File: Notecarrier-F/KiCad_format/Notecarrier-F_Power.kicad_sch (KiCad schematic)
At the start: 48 parts, among them J1 S2BPHSM4TBLFSN, J2 S2BPHSM4TBLFSN, J3 S2BPHSM4TBLFSN, J4 10118193-0001LF, U1 TPS62748YFPT, U2 BQ24210DQCT, U3 TPS63020DSJR, U5 MAX17225ELT+

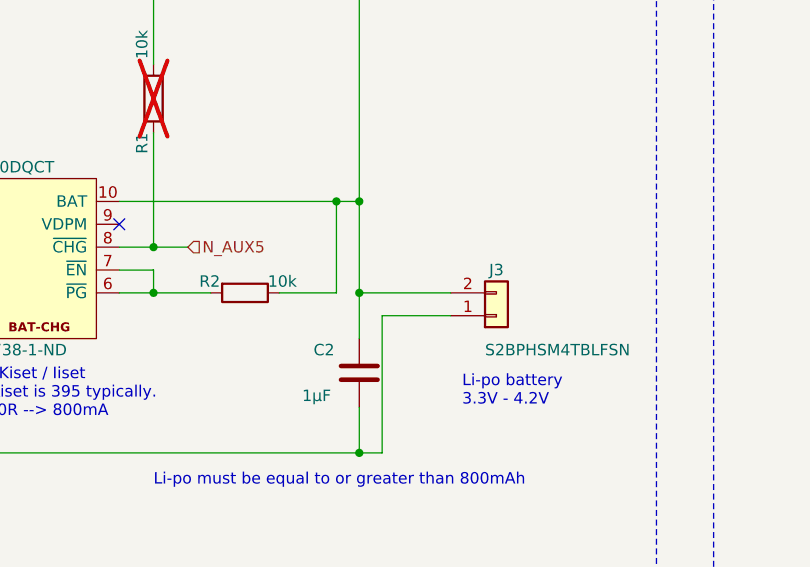
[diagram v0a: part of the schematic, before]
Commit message: Correct BQ24210DQCT BAT pin to Power Input.
Realised it was incorrectly specified as a Power Output while porting Notecarrier-A. It’s the battery itself which is the source of power, so even though this pin provides charging current, it must be a Power Input since it is connected to the Power Output of the battery. The symbol has been fixed, so I updated it and put the PWR_FLAG where it should be - at the battery.
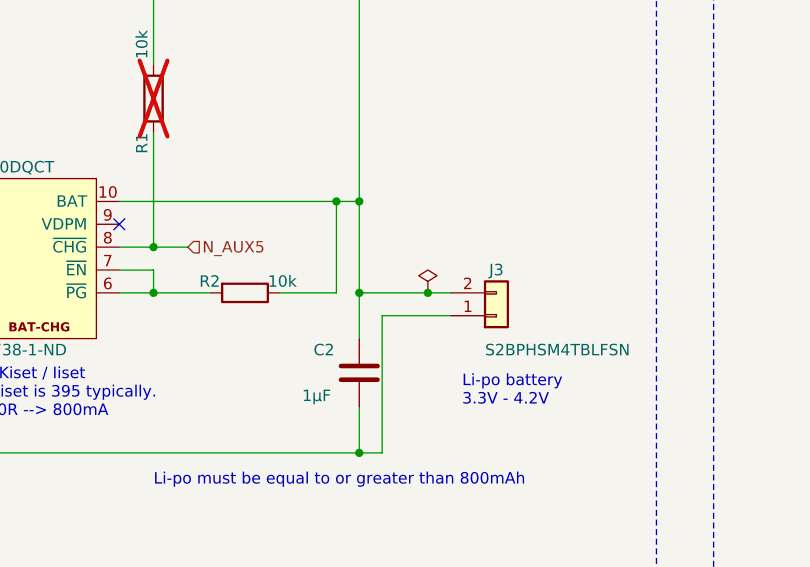
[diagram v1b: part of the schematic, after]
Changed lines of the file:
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@@
   (junction (at 257.81 71.12) (diameter 0) (color 0 0 0 0)
+  )
+  (junction (at 153.67 135.89) (diameter 0) (color 0 0 0 0)
   )
   (junction (at 309.88 170.18) (diameter 0) (color 0 0 0 0)
@@
     (stroke (width 0) (type default))
   )
-  (wire (pts (xy 146.05 135.89) (xy 156.21 135.89))
+  (wire (pts (xy 146.05 135.89) (xy 153.67 135.89))
     (stroke (width 0) (type default))
   )
@@
   )
   (wire (pts (xy 322.58 160.02) (xy 313.69 160.02))
+    (stroke (width 0) (type default))
+  )
+  (wire (pts (xy 153.67 135.89) (xy 156.21 135.89))
     (stroke (width 0) (type default))
   )
@@
         )
       )
+    )
+  )
+  (symbol (lib_id "power:PWR_FLAG") (at 153.67 135.89 0) (unit 1)
+    (in_bom yes) (on_board yes) (dnp no) (fields_autoplaced)
+    (property "Reference" "#FLG012" (at 153.67 133.985 0)
+      (effects (font (size 1.27 1.27)) hide)
+    )
+    (property "Value" "PWR_FLAG" (at 153.67 132.08 0)
+      (effects (font (size 1.27 1.27)) hide)
+    )
+    (property "Footprint" "" (at 153.67 135.89 0)
+      (effects (font (size 1.27 1.27)) hide)
+    )
+    (property "Datasheet" "~" (at 153.67 135.89 0)
+      (effects (font (size 1.27 1.27)) hide)
+    )
+    (property "Critical" "" (at 153.67 135.89 0)
+      (effects (font (size 1.27 1.27)) hide)
+    )
+    (property "Description" "" (at 153.67 135.89 0)
+      (effects (font (size 1.27 1.27)) hide)
+    )
+    (property "Manufacturer" "" (at 153.67 135.89 0)
+      (effects (font (size 1.27 1.27)) hide)
+    )
+    (property "Order Code" "" (at 153.67 135.89 0)
+      (effects (font (size 1.27 1.27)) hide)
+    )
+    (property "Part Number" "" (at 153.67 135.89 0)
+      (effects (font (size 1.27 1.27)) hide)
+    )
+    (property "Supplier" "" (at 153.67 135.89 0)
+      (effects (font (size 1.27 1.27)) hide)
+    )
+    (pin "1")
+    (instances
+      (project "Notecarrier-F"
+        (path "/3e57c059-f782-40ac-b9a3-c1636ed27a63/88418874-7972-4492-bdff-7ad1935acea6"
+          (reference "#FLG012") (unit 1)
+        )
+      )
